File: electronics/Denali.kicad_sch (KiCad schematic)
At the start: 0 parts

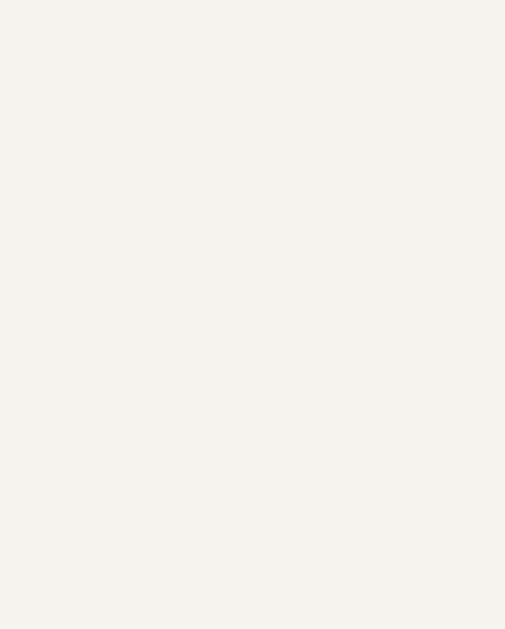
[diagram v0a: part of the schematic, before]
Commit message: add kb2040 to schem and add io exp and switch
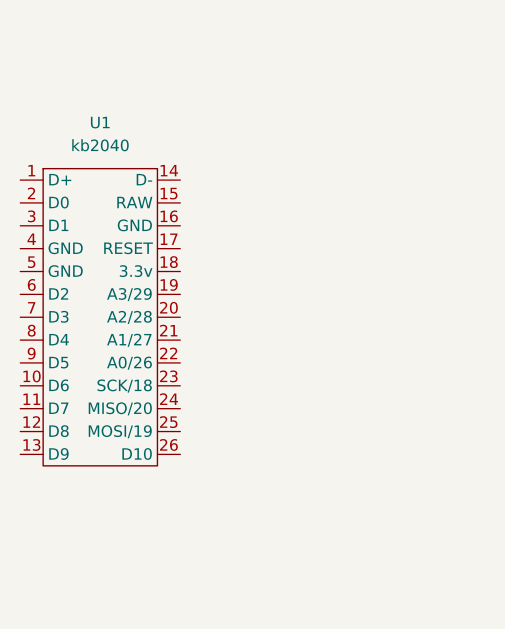
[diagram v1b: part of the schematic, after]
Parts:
- added U1: kb2040, KeeBoar:kb2040, symbol kb2040:kb2040
